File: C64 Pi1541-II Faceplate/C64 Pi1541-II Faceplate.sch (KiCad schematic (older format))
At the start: 8 parts, among them IC1 0.96_OLED, J4 Faceplate, M1 Mounting, M2 Mounting, M3 Mounting, M4 Mounting

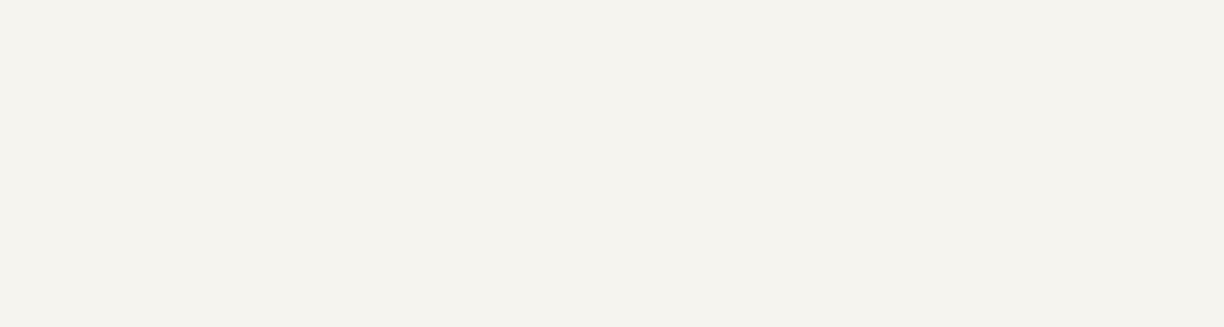
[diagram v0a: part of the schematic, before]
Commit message: Added DIN cutout
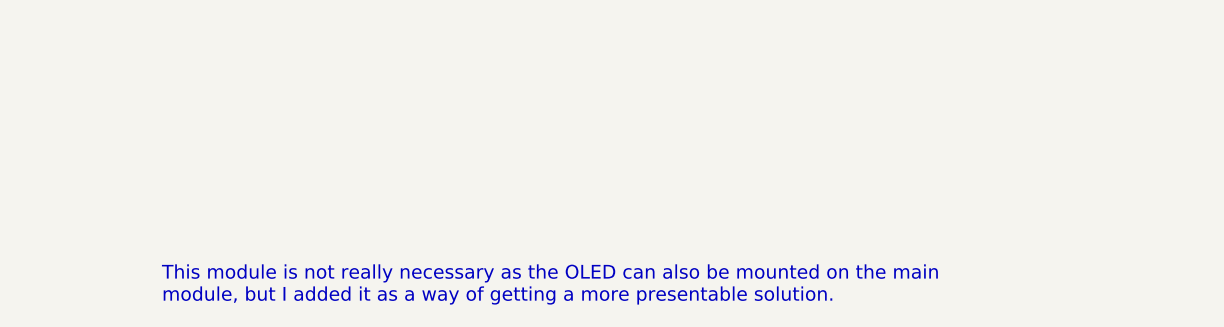
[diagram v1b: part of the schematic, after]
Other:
- note added: "This module is not really necessary as the OLED can also be mounted on the main\nmodule, but I added it as a way of getting a more presentable solution."
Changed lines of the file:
@@
 	-1   0    0    -1
 $EndComp
+Text Notes 7000 6750 0    60   ~ 0
+This module is not really necessary as the OLED can also be mounted on the main\nmodule, but I added it as a way of getting a more presentable solution.
 $EndSCHEMATC
